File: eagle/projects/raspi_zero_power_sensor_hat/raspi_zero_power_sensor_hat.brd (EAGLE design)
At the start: 65 x 30 mm, 158 parts, among them J301 MOL-SL-2-RA, J302 USB_MICROB_RECPT, J401 MOL-SL-2-RA, J402 MOL-SL-2-V, J601 RECEPTACLE-2x5-2.54MM, J602 MOL-SL-4-RA, J603 MOL-SL-3-V, J604 RECEPTACLE-2x3-2.54MM, Q301 SSM6N7002KFU, Q401 SSM6N7002KFU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

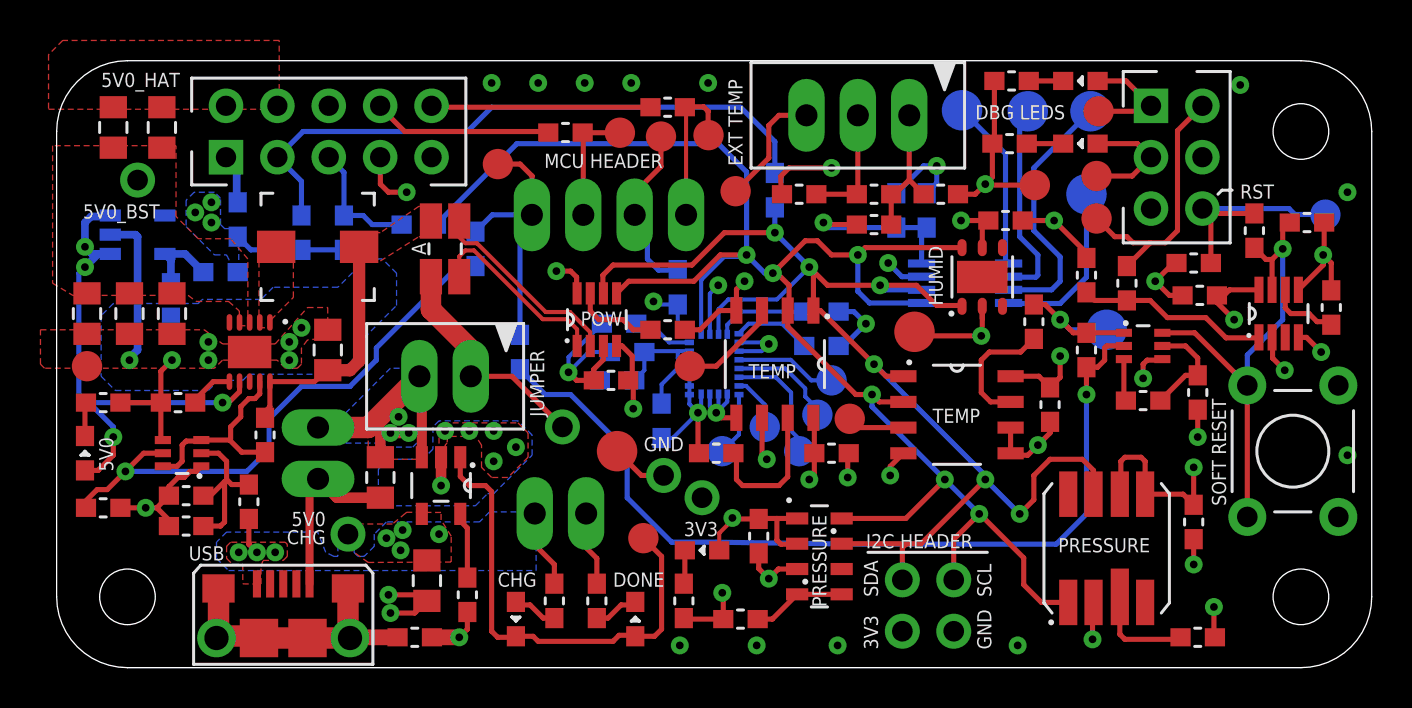
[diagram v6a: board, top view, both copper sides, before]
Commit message: cleaned up traces for perpendicular pad entry
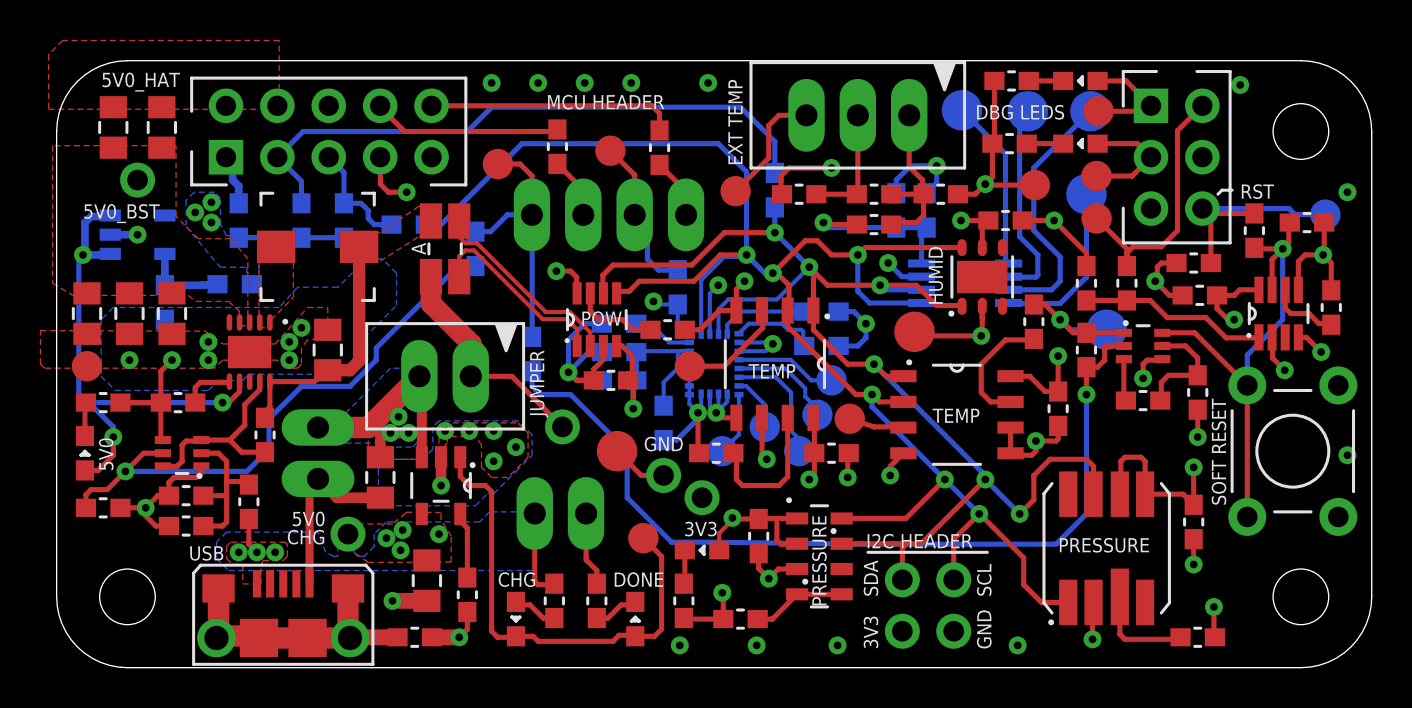
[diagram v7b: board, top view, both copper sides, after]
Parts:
- removed TP607, TP608: (no value), daqcs:TP15R
- moved TP610 2.60 mm to (27.4, 25.6)
- moved R610 2.04 mm to (29.8, 25.7), turned to 270 degrees
- moved R401 0.92 mm to (8.80, 18.9)
- moved R609 0.81 mm to (24.8, 25.8), turned to 270 degrees
- moved R612 0.61 mm to (23.5, 15.5)
- moved R603 0.60 mm to (12.1, 22.1)
- moved R604 0.60 mm to (14.2, 22.1)
- moved R602 0.50 mm to (17.4, 21.9)
- moved C501 0.45 mm to (49.5, 12.8)
- moved C507 0.40 mm to (27.8, 15.6)
- moved R309 0.40 mm to (50.9, 19.0)
- moved C402 0.32 mm to (5.35, 18.1)
- moved C505 0.14 mm to (30.0, 12.1)
- moved C509 0.10 mm to (27.8, 14.2)
- moved R606 0.07 mm to (9.00, 22.1)
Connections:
- net PP3V3_HAT renamed NFO
- net UART_RASPI_RXD_MCU_TXD: no longer TP607.TP
- net UART_RASPI_TXD_MCU_RXD: no longer TP608.TP
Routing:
- net GND: track 146.4 -> 140.9 mm
- net UART_RASPI_RXD_MCU_TXD: track 8.03 -> 3.01 mm
- net UART_RASPI_TXD_MCU_RXD: track 5.93 -> 3.05 mm
- net NFO: track 76.5 -> 78.6 mm
- net PP3V3_TEMP: track 6.88 -> 8.78 mm
- net UART_RASPI_RXD_MCU_TXD_R: track 10.8 -> 12.3 mm
- net I2C1_RASPI_SDA: track 67.0 -> 67.7 mm
- net I2C1_RASPI_SCL_R: track 6.23 -> 5.61 mm
- net I2C1_RASPI_SDA_R: track 31.2 -> 30.6 mm
- net PP5V0_BST: track 25.6 -> 25.0 mm, vias 4 -> 3
- net PP5V0_CHG_IN: track 5.69 -> 6.23 mm
- net MCU_TO_BST_RESET: track 27.9 -> 28.4 mm
- net I2C1_RASPI_SCL: track 88.0 -> 88.5 mm
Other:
- board text added: "3V3_HAT"

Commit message: somehow PP3V3_HAT got renamed to NFO???
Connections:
- net NFO renamed PP3V3_HAT
